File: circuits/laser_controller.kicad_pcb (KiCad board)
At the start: 4 copper layers, 173 x 61.1 mm, 180 parts, among them J1 USB_MINI_B, J2 USB_MINI_B, J5 24V DC IN, J6 CONN_RJ45, Q1 SOT-23, Q2 SOT-23, Q3 SOT-23, Q4 SOT-23, Q5 SOT-23, Q6 SOT-23, SW1 SW_PUSH, SW2 SW_PUSH, SW3 SW_PUSH, U1 SOIC-8_3.9x4.9mm_P1.27mm, U10 QFN-28-1EP_5x5mm_P0.5mm_EP3.3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, U11 SOT-23-5, U12 TSSOP-14_4.4x5mm_P0.65mm, U13 SOT-23, U14 LQFP-64_10x10mm_P0.5mm, U15 TSOT-23-6, U16 TSOT-23-6, U2 SOIC-8_3.9x4.9mm_P1.27mm, U3 SOIC-8_3.9x4.9mm_P1.27mm, U4 SOIC-8_3.9x4.9mm_P1.27mm, U5 SOT-23-5, U6 SOT-23-5, U7 SOT-23-5, U8 SOT-23-5, U9 ESP32-S3-WROOM-1

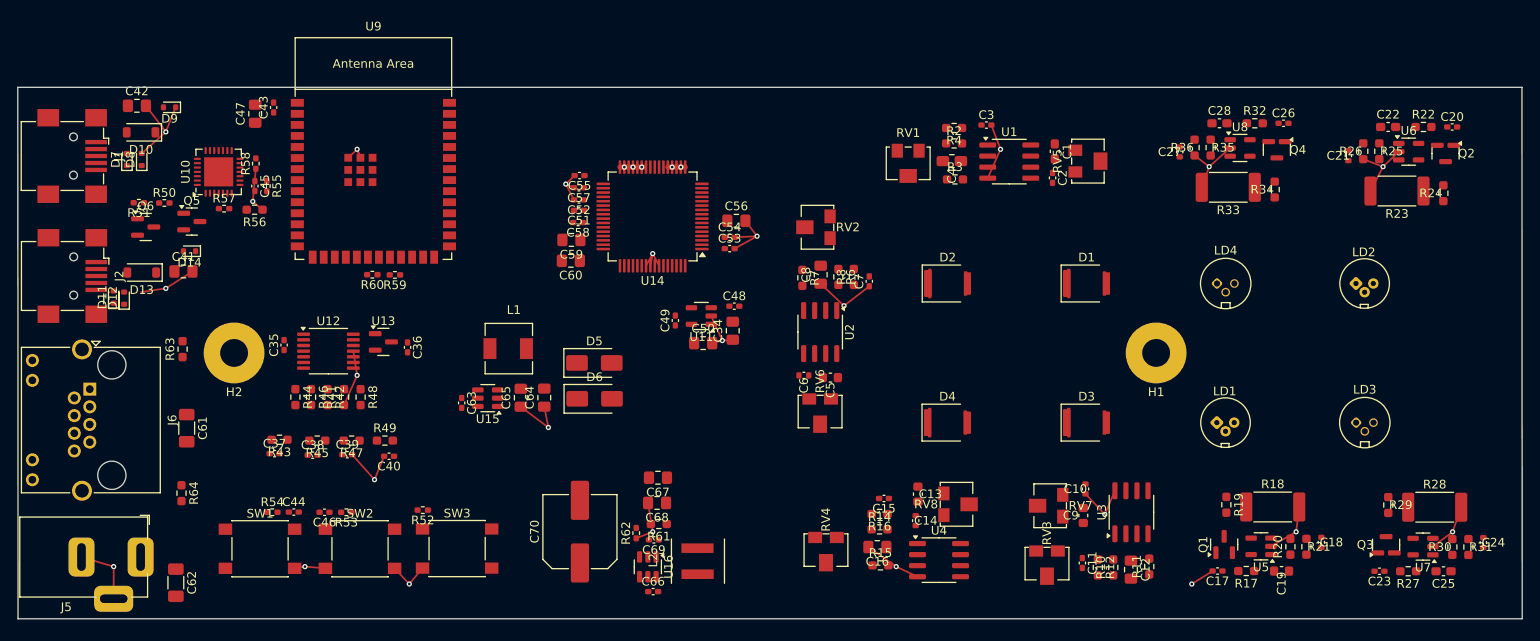
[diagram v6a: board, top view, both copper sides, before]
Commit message: Remove GND fanout traces — keep vias only, zone pour handles connections (AC pattern)
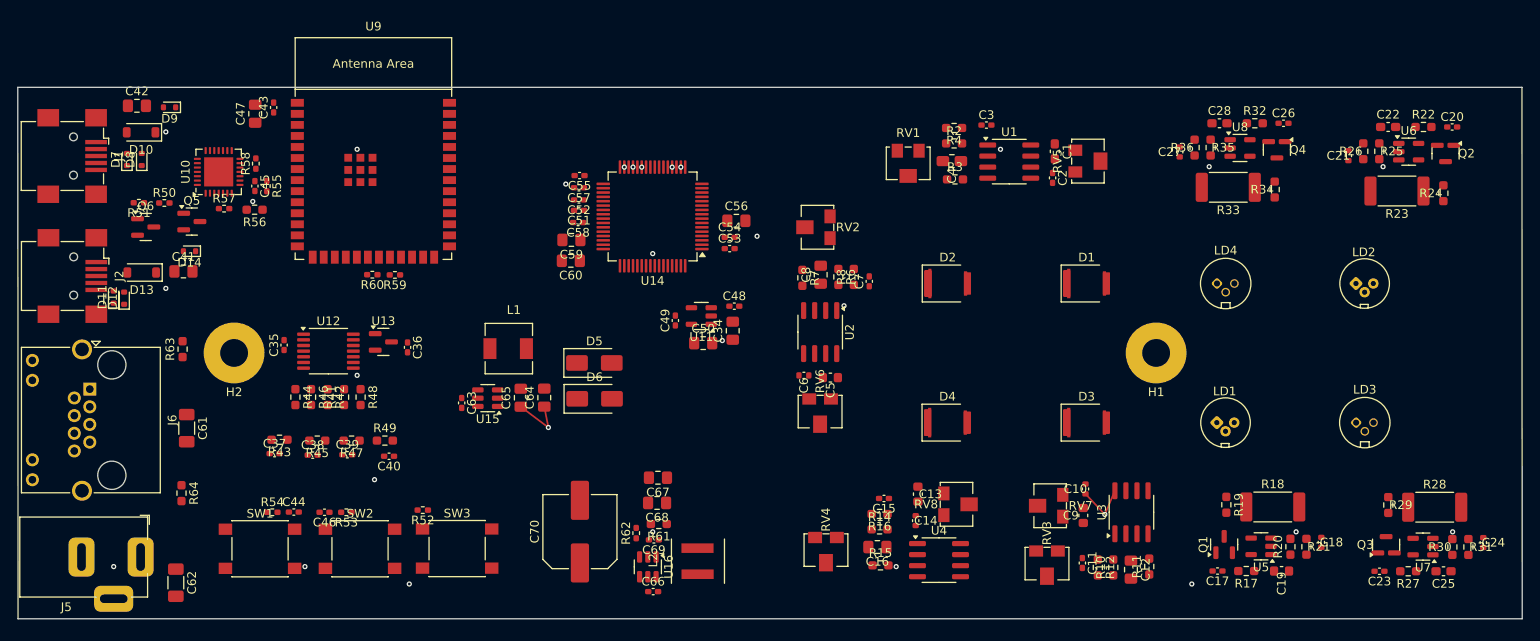
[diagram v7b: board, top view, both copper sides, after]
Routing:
- net GND: track 139.1 -> 0.00 mm
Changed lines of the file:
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@@
   (segment (start 88.825 116.6125) (end 92 119) (width 0.2) (layer "F.Cu") (net 33))
   (via (at 92 119) (size 0.6) (drill 0.3) (layers "F.Cu" "B.Cu") (net 33))
-  (segment (start 123.3175 102.465) (end 126 105) (width 0.2) (layer "F.Cu") (net 46))
-  (segment (start 45.225 87.475) (end 48 85) (width 0.2) (layer "F.Cu") (net 46))
-  (segment (start 103.2325 100.4) (end 104 99) (width 0.2) (layer "F.Cu") (net 46))
-  (segment (start 110.7275 106.175) (end 112 109) (width 0.2) (layer "F.Cu") (net 46))
-  (segment (start 175.1025 132.6675) (end 178 131) (width 0.2) (layer "F.Cu") (net 46))
-  (segment (start 68.5 116.4175) (end 70 113) (width 0.2) (layer "F.Cu") (net 46))
-  (segment (start 134.45 136.16) (end 132 135) (width 0.2) (layer "F.Cu") (net 46))
-  (segment (start 59.1225 93.95) (end 58 93) (width 0.2) (layer "F.Cu") (net 46))
-  (segment (start 62.8125 135.2) (end 64 135) (width 0.2) (layer "F.Cu") (net 46))
-  (segment (start 45.15 103.425) (end 48 103) (width 0.2) (layer "F.Cu") (net 46))
-  (segment (start 38.3 133.9) (end 42 135) (width 0.2) (layer "F.Cu") (net 46))
-  (segment (start 114.6575 95.225) (end 116 97) (width 0.2) (layer "F.Cu") (net 46))
-  (segment (start 94.9475 92.825) (end 94 91) (width 0.2) (layer "F.Cu") (net 46))
-  (segment (start 70.375 87.975) (end 70 87) (width 0.2) (layer "F.Cu") (net 46))
-  (segment (start 103.4625 127.675) (end 104 131) (width 0.2) (layer "F.Cu") (net 46))
-  (segment (start 73.105 122.305) (end 72 125) (width 0.2) (layer "F.Cu") (net 46))
-  (segment (start 185.724 88.1405) (end 188 89) (width 0.2) (layer "F.Cu") (net 46))
-  (segment (start 95.015 90.025) (end 94 91) (width 0.2) (layer "F.Cu") (net 46))
-  (segment (start 128.9055 102.757) (end 126 105) (width 0.2) (layer "F.Cu") (net 46))
-  (segment (start 66.3525 135.2) (end 64 135) (width 0.2) (layer "F.Cu") (net 46))
-  (segment (start 70.375 87.975) (end 70 87) (width 0.2) (layer "F.Cu") (net 46))
-  (segment (start 68.975 87.975) (end 70 87) (width 0.2) (layer "F.Cu") (net 46))
-  (segment (start 166.324 87.7155) (end 168 89) (width 0.2) (layer "F.Cu") (net 46))
-  (segment (start 113.4175 98.425) (end 116 97) (width 0.2) (layer "F.Cu") (net 46))
-  (segment (start 186.55 91.8) (end 188 89) (width 0.2) (layer "F.Cu") (net 46))
-  (segment (start 113.2025 108.9075) (end 112 109) (width 0.2) (layer "F.Cu") (net 46))
-  (segment (start 69.5625 110.2175) (end 70 113) (width 0.2) (layer "F.Cu") (net 46))
-  (segment (start 193.7295 132.6955) (end 196 131) (width 0.2) (layer "F.Cu") (net 46))
-  (segment (start 74.3125 135.2) (end 76 137) (width 0.2) (layer "F.Cu") (net 46))
-  (segment (start 167.15 91.375) (end 168 89) (width 0.2) (layer "F.Cu") (net 46))
-  (segment (start 103.7325 100.4) (end 104 99) (width 0.2) (layer "F.Cu") (net 46))
-  (segment (start 113.4175 97.125) (end 116 97) (width 0.2) (layer "F.Cu") (net 46))
-  (segment (start 142.531 90.3225) (end 144 87) (width 0.2) (layer "F.Cu") (net 46))
-  (segment (start 49.125 82.175) (end 48 85) (width 0.2) (layer "F.Cu") (net 46))
-  (segment (start 58.35 89.245) (end 58 93) (width 0.2) (layer "F.Cu") (net 46))
-  (segment (start 178.361 128.1415) (end 178 131) (width 0.2) (layer "F.Cu") (net 46))
-  (segment (start 69.44 122.13) (end 72 125) (width 0.2) (layer "F.Cu") (net 46))
-  (segment (start 189.8085 87.274) (end 188 89) (width 0.2) (layer "F.Cu") (net 46))
-  (segment (start 168.3935 135.5075) (end 166 137) (width 0.2) (layer "F.Cu") (net 46))
-  (segment (start 170.4085 86.849) (end 168 89) (width 0.2) (layer "F.Cu") (net 46))
-  (segment (start 104.7325 100.4) (end 104 99) (width 0.2) (layer "F.Cu") (net 46))
-  (segment (start 196.988 128.1695) (end 196 131) (width 0.2) (layer "F.Cu") (net 46))
-  (segment (start 128.8 132.75) (end 132 135) (width 0.2) (layer "F.Cu") (net 46))
-  (segment (start 77.5225 135.175) (end 76 137) (width 0.2) (layer "F.Cu") (net 46))
-  (segment (start 94.9475 91.425) (end 94 91) (width 0.2) (layer "F.Cu") (net 46))
-  (segment (start 42 138.7) (end 42 135) (width 0.2) (layer "F.Cu") (net 46))
-  (segment (start 51.0625 101.05) (end 48 103) (width 0.2) (layer "F.Cu") (net 46))
-  (segment (start 142.948 84.216) (end 144 87) (width 0.2) (layer "F.Cu") (net 46))
-  (segment (start 102.1 131.745) (end 104 131) (width 0.2) (layer "F.Cu") (net 46))
-  (segment (start 45.7125 82) (end 48 85) (width 0.2) (layer "F.Cu") (net 46))
-  (segment (start 110.84 109.295) (end 112 109) (width 0.2) (layer "F.Cu") (net 46))
-  (segment (start 106.2325 89.05) (end 106.7325 89.05) (width 0.6) (layer "F.Cu") (net 46))
-  (segment (start 101.2325 89.05) (end 101.7325 89.05) (width 0.6) (layer "F.Cu") (net 46))
-  (segment (start 101.2325 89.05) (end 100.7325 89.05) (width 0.6) (layer "F.Cu") (net 46))
-  (segment (start 102.7325 89.05) (end 103.0325 89.05) (width 0.6) (layer "F.Cu") (net 46))
-  (segment (start 105.7325 89.05) (end 106.2325 89.05) (width 0.6) (layer "F.Cu") (net 46))
-  (segment (start 107.7325 89.05) (end 107.2325 89.05) (width 0.6) (layer "F.Cu") (net 46))
-  (segment (start 102.2325 89.05) (end 101.7325 89.05) (width 0.6) (layer "F.Cu") (net 46))
-  (segment (start 100.2325 89.05) (end 100.7325 89.05) (width 0.6) (layer "F.Cu") (net 46))
-  (segment (start 102.2325 89.05) (end 102.7325 89.05) (width 0.6) (layer "F.Cu") (net 46))
-  (segment (start 106.7325 89.05) (end 107.2325 89.05) (width 0.6) (layer "F.Cu") (net 46))
   (via (at 188 89) (size 0.6) (drill 0.3) (layers "F.Cu" "B.Cu") (net 46))
   (via (at 104 131) (size 0.6) (drill 0.3) (layers "F.Cu" "B.Cu") (net 46))

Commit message: Remove all auto-generated routing — zero segments/vias, zero overlaps, clean base for manual routing
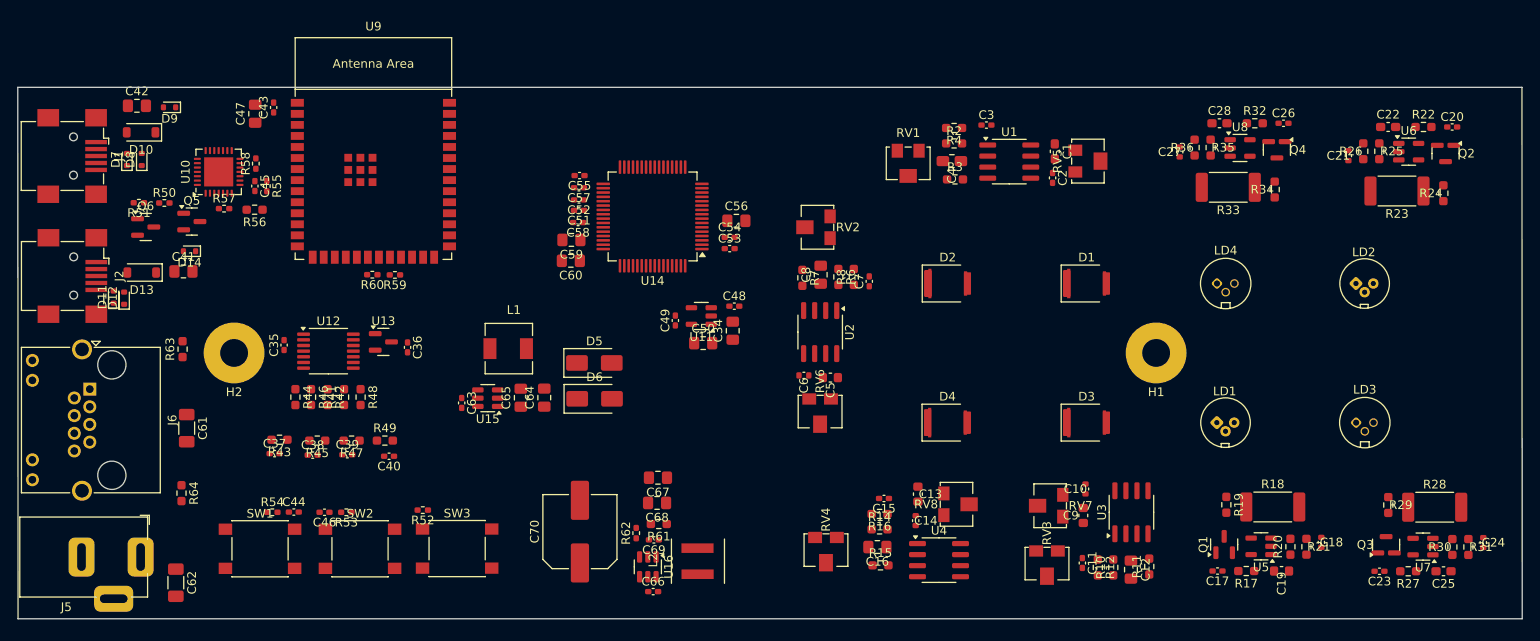
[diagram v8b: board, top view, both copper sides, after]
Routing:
- net /POWER_IO/BUCK_5V: track 6.42 -> 0.00 mm, vias 1 -> 0
- net +5V: track 6.21 -> 0.00 mm, vias 1 -> 0
- net GND: vias 27 -> 0
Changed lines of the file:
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@@
     (effects (font (size 1.2 1.2) (thickness 0.18)))
   )
-  (segment (start 157.155 126.275) (end 156 129) (width 0.2) (layer "F.Cu") (net 2))
-  (segment (start 153.7755 126.635) (end 156 129) (width 0.2) (layer "F.Cu") (net 2))
-  (via (at 156 129) (size 0.6) (drill 0.3) (layers "F.Cu" "B.Cu") (net 2))
-  (segment (start 91.525 116.6) (end 92 119) (width 0.2) (layer "F.Cu") (net 33))
-  (segment (start 88.825 116.6125) (end 92 119) (width 0.2) (layer "F.Cu") (net 33))
-  (via (at 92 119) (size 0.6) (drill 0.3) (layers "F.Cu" "B.Cu") (net 33))
-  (via (at 188 89) (size 0.6) (drill 0.3) (layers "F.Cu" "B.Cu") (net 46))
-  (via (at 104 131) (size 0.6) (drill 0.3) (layers "F.Cu" "B.Cu") (net 46))
-  (via (at 132 135) (size 0.6) (drill 0.3) (layers "F.Cu" "B.Cu") (net 46))
-  (via (at 116 97) (size 0.6) (drill 0.3) (layers "F.Cu" "B.Cu") (net 46))
-  (via (at 48 85) (size 0.6) (drill 0.3) (layers "F.Cu" "B.Cu") (net 46))
-  (via (at 70 87) (size 0.6) (drill 0.3) (layers "F.Cu" "B.Cu") (net 46))
-  (via (at 126 105) (size 0.6) (drill 0.3) (layers "F.Cu" "B.Cu") (net 46))
-  (via (at 144 87) (size 0.6) (drill 0.3) (layers "F.Cu" "B.Cu") (net 46))
-  (via (at 48 103) (size 0.6) (drill 0.3) (layers "F.Cu" "B.Cu") (net 46))
-  (via (at 94 91) (size 0.6) (drill 0.3) (layers "F.Cu" "B.Cu") (net 46))
-  (via (at 58 93) (size 0.6) (drill 0.3) (layers "F.Cu" "B.Cu") (net 46))
-  (via (at 112 109) (size 0.6) (drill 0.3) (layers "F.Cu" "B.Cu") (net 46))
-  (via (at 42 135) (size 0.6) (drill 0.3) (layers "F.Cu" "B.Cu") (net 46))
-  (via (at 196 131) (size 0.6) (drill 0.3) (layers "F.Cu" "B.Cu") (net 46))
-  (via (at 72 125) (size 0.6) (drill 0.3) (layers "F.Cu" "B.Cu") (net 46))
-  (via (at 104 99) (size 0.6) (drill 0.3) (layers "F.Cu" "B.Cu") (net 46))
-  (via (at 64 135) (size 0.6) (drill 0.3) (layers "F.Cu" "B.Cu") (net 46))
-  (via (at 168 89) (size 0.6) (drill 0.3) (layers "F.Cu" "B.Cu") (net 46))
-  (via (at 178 131) (size 0.6) (drill 0.3) (layers "F.Cu" "B.Cu") (net 46))
-  (via (at 70 113) (size 0.6) (drill 0.3) (layers "F.Cu" "B.Cu") (net 46))
-  (via (at 76 137) (size 0.6) (drill 0.3) (layers "F.Cu" "B.Cu") (net 46))
-  (via (at 166 137) (size 0.6) (drill 0.3) (layers "F.Cu" "B.Cu") (net 46))
-  (via (at 107.2325 89.05) (size 0.6) (drill 0.3) (layers "F.Cu" "B.Cu") (net 46))
-  (via (at 100.7325 89.05) (size 0.6) (drill 0.3) (layers "F.Cu" "B.Cu") (net 46))
-  (via (at 102.7325 89.05) (size 0.6) (drill 0.3) (layers "F.Cu" "B.Cu") (net 46))
-  (via (at 106.2325 89.05) (size 0.6) (drill 0.3) (layers "F.Cu" "B.Cu") (net 46))
-  (via (at 101.7325 89.05) (size 0.6) (drill 0.3) (layers "F.Cu" "B.Cu") (net 46))
   (zone (net 46) (net_name "GND") (layer "In1.Cu") (hatch edge 0.508)
     (connect_pads (clearance 0.508))
